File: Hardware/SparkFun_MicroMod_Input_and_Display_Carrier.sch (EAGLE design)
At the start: 69 parts, among them J1 MICROMOD-2222-C, J2 MICRO-SD, J3 USB-C_Prog, J4 AVR_SPI_PROG_3X2TESTPOINTS, J5 2.4" TFT, J6 QWIIC_RA, J7 CORTEX_JTAG_DEBUG, Q1 1.1A/600mΩ, Q2 600mA/40V, U2 ATTINY84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

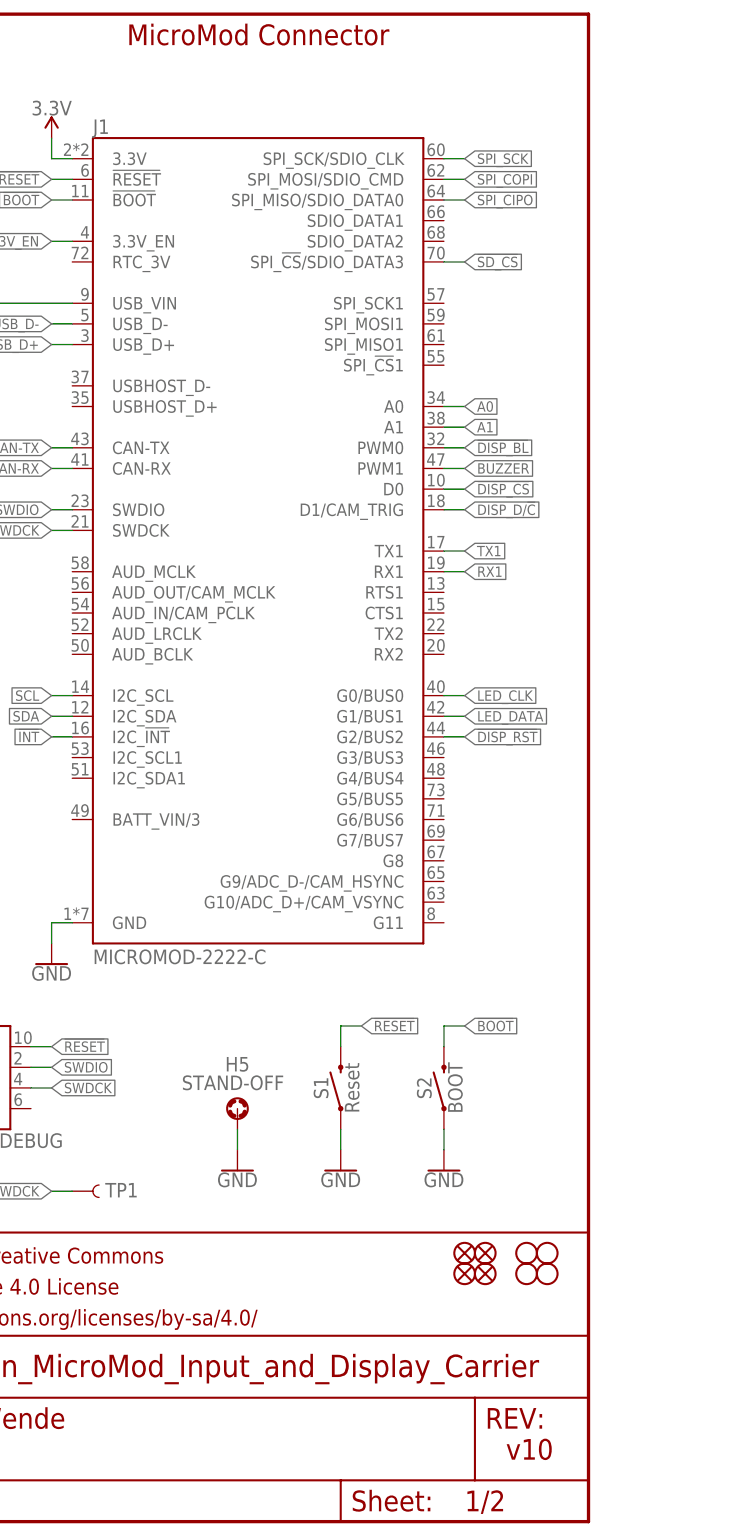
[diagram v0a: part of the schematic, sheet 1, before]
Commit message: v11
Updated MM conenctor SPI pins
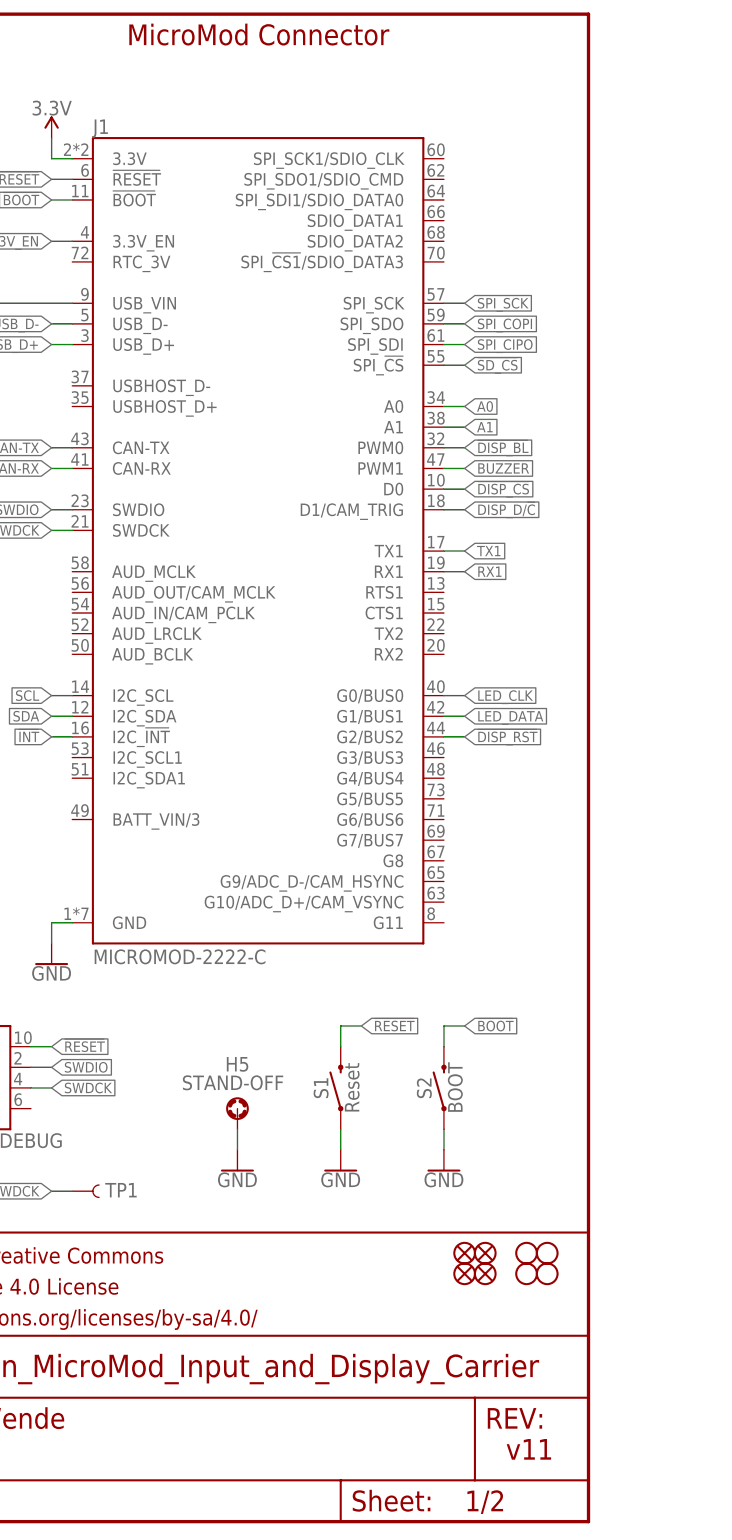
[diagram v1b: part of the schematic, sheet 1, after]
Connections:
- net !SD_CS: now also J1.SPI_!CS!; no longer J1.SPI_!CS!/SDIO_DATA3
- net SPI_CIPO: now also J1.SPI_SDI; no longer J1.SPI_MISO/SDIO_DATA0
- net SPI_COPI: now also J1.SPI_SDO; no longer J1.SPI_MOSI/SDIO_CMD
- net SPI_SCK: now also J1.SPI_SCK; no longer J1.SPI_SCK/SDIO_CLK
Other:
- note added: "v11"
- note removed: "v10"
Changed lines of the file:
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@@
 <text x="83.82" y="83.82" size="1.27" layer="97" font="vector">7-bit Unshifted I2C Address: 0x71</text>
 <text x="165.862" y="11.43" size="2.54" layer="94" font="vector">Alex Wende</text>
-<text x="238.76" y="7.62" size="2.54" layer="94" font="vector">v10</text>
+<text x="238.76" y="7.62" size="2.54" layer="94" font="vector">v11</text>
 <wire x1="0" y1="78.74" x2="88.9" y2="78.74" width="0.2032" layer="97" style="longdash"/>
 <wire x1="88.9" y1="78.74" x2="147.32" y2="78.74" width="0.2032" layer="97" style="longdash"/>
@@
 <net name="SPI_SCK" class="0">
 <segment>
-<pinref part="J1" gate="J1" pin="SPI_SCK/SDIO_CLK"/>
-<wire x1="231.14" y1="167.64" x2="233.68" y2="167.64" width="0.1524" layer="91"/>
-<label x="233.68" y="167.64" size="1.27" layer="95" font="vector" xref="yes"/>
-</segment>
-<segment>
 <pinref part="J2" gate="J1" pin="SCK"/>
 <wire x1="111.76" y1="43.18" x2="101.6" y2="43.18" width="0.1524" layer="91"/>
@@
 <label x="58.42" y="43.18" size="1.27" layer="95" font="vector" xref="yes"/>
 </segment>
+<segment>
+<pinref part="J1" gate="J1" pin="SPI_SCK"/>
+<wire x1="231.14" y1="149.86" x2="233.68" y2="149.86" width="0.1524" layer="91"/>
+<label x="233.68" y="149.86" size="1.27" layer="95" xref="yes"/>
+</segment>
 </net>
 <net name="SPI_COPI" class="0">
-<segment>
-<pinref part="J1" gate="J1" pin="SPI_MOSI/SDIO_CMD"/>
-<wire x1="231.14" y1="165.1" x2="233.68" y2="165.1" width="0.1524" layer="91"/>
-<label x="233.68" y="165.1" size="1.27" layer="95" font="vector" xref="yes"/>
-</segment>
 <segment>
 <pinref part="J2" gate="J1" pin="DI"/>
@@
 <label x="58.42" y="48.26" size="1.27" layer="95" font="vector" xref="yes"/>
 </segment>
+<segment>
+<pinref part="J1" gate="J1" pin="SPI_SDO"/>
+<wire x1="231.14" y1="147.32" x2="233.68" y2="147.32" width="0.1524" layer="91"/>
+<label x="233.68" y="147.32" size="1.27" layer="95" xref="yes"/>
+</segment>
 </net>
 <net name="SPI_CIPO" class="0">
-<segment>
-<pinref part="J1" gate="J1" pin="SPI_MISO/SDIO_DATA0"/>
-<wire x1="231.14" y1="162.56" x2="233.68" y2="162.56" width="0.1524" layer="91"/>
-<label x="233.68" y="162.56" size="1.27" layer="95" font="vector" xref="yes"/>
-</segment>
 <segment>
 <pinref part="J2" gate="J1" pin="DO"/>
@@
 <label x="58.42" y="35.56" size="1.27" layer="95" font="vector" xref="yes"/>
 </segment>
+<segment>
+<pinref part="J1" gate="J1" pin="SPI_SDI"/>
+<wire x1="231.14" y1="144.78" x2="233.68" y2="144.78" width="0.1524" layer="91"/>
+<label x="233.68" y="144.78" size="1.27" layer="95" xref="yes"/>
+</segment>
 </net>
 <net name="!SD_CS" class="0">
-<segment>
-<pinref part="J1" gate="J1" pin="SPI_!CS!/SDIO_DATA3"/>
-<wire x1="231.14" y1="154.94" x2="233.68" y2="154.94" width="0.1524" layer="91"/>
-<label x="233.68" y="154.94" size="1.27" layer="95" font="vector" xref="yes"/>
-</segment>
 <segment>
 <pinref part="J2" gate="J1" pin="CS"/>
@@
 <junction x="104.14" y="50.8"/>
 </segment>
+<segment>
+<pinref part="J1" gate="J1" pin="SPI_!CS!"/>
+<wire x1="231.14" y1="142.24" x2="233.68" y2="142.24" width="0.1524" layer="91"/>
+<label x="233.68" y="142.24" size="1.27" layer="95" xref="yes"/>
+</segment>
 </net>
